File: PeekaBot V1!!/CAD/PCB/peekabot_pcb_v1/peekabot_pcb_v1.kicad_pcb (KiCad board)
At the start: 2 copper layers, 25 parts, among them J1 esp32camright, J2 esp32camleft, J3 USB_B_Micro, J4 Battery Socket, SW1 SW_Push, SW2 SW_Push, U1 IP5306

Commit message: UPDATED PCB-MARK-1!!!
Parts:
- added REF**: M2, MountingHole:MountingHole_2.2mm_M2, F.Cu at (128.5, 56.0)
- added REF**: M2, MountingHole:MountingHole_2.2mm_M2, F.Cu at (156.5, 56.0)
- added REF**: M2, MountingHole:MountingHole_2.2mm_M2, F.Cu at (128.5, 99.5)
- added REF**: M2, MountingHole:MountingHole_2.2mm_M2, F.Cu at (156.5, 99.5)
- moved D3 33.0 mm to (150.0, 67.0), turned to 90 degrees
- moved D2 31.0 mm to (144.0, 63.5)
- moved KEY 24.9 mm to (135.4, 98.8)
- moved J4 23.9 mm to (134.8, 61.0)
- moved R5 23.4 mm to (135.9, 79.5), turned to 180 degrees
- moved J3 22.3 mm to (149.0, 56.7), turned to 180 degrees
- moved C7 18.8 mm to (136.0, 77.0)
- moved J1 18.8 mm to (153.0, 67.0)
- moved J2 17.8 mm to (131.5, 84.5), turned to 180 degrees
- moved U1 17.1 mm to (142.7, 68.1), turned to 180 degrees
- moved IO0 16.6 mm to (150.6, 99.2)
- moved R2 16.2 mm to (145.0, 72.5)
- moved R3 13.7 mm to (140.0, 85.0), turned to 180 degrees
- moved C6 12.0 mm to (135.9, 74.5), turned to 180 degrees
- moved C4 11.9 mm to (136.0, 66.5)
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- renumbered SW1 to IO0, SW2 to KEY
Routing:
- net GND: track 0.00 -> 99.4 mm, vias 0 -> 1
- net BAT: track 0.00 -> 46.8 mm, vias 0 -> 5
- net (no net): track 0.00 -> 44.9 mm, vias 0 -> 7
- net io0: track 0.00 -> 33.7 mm
- net 5V: track 0.00 -> 29.4 mm, vias 0 -> 2
- net Net-(U1-KEY): track 0.00 -> 22.2 mm
- net Net-(R4-Pad2): track 0.00 -> 20.2 mm
- net Net-(J3-VBUS): track 0.00 -> 19.8 mm
- net Net-(U1-SW): track 0.00 -> 12.9 mm, vias 0 -> 2
- net Net-(C5-Pad1): track 0.00 -> 12.6 mm
- net Net-(D3-A): track 0.00 -> 7.99 mm, vias 0 -> 2
- net VCC: track 0.00 -> 7.08 mm
- net Net-(D2-A): track 0.00 -> 6.49 mm
- net Net-(C7-Pad1): track 0.00 -> 2.54 mm
- net Net-(D1-A): track 0.00 -> 2.18 mm
- added copper zone on F.Cu, net GND
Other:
- board outline added: 34.5 x 49.5 mm

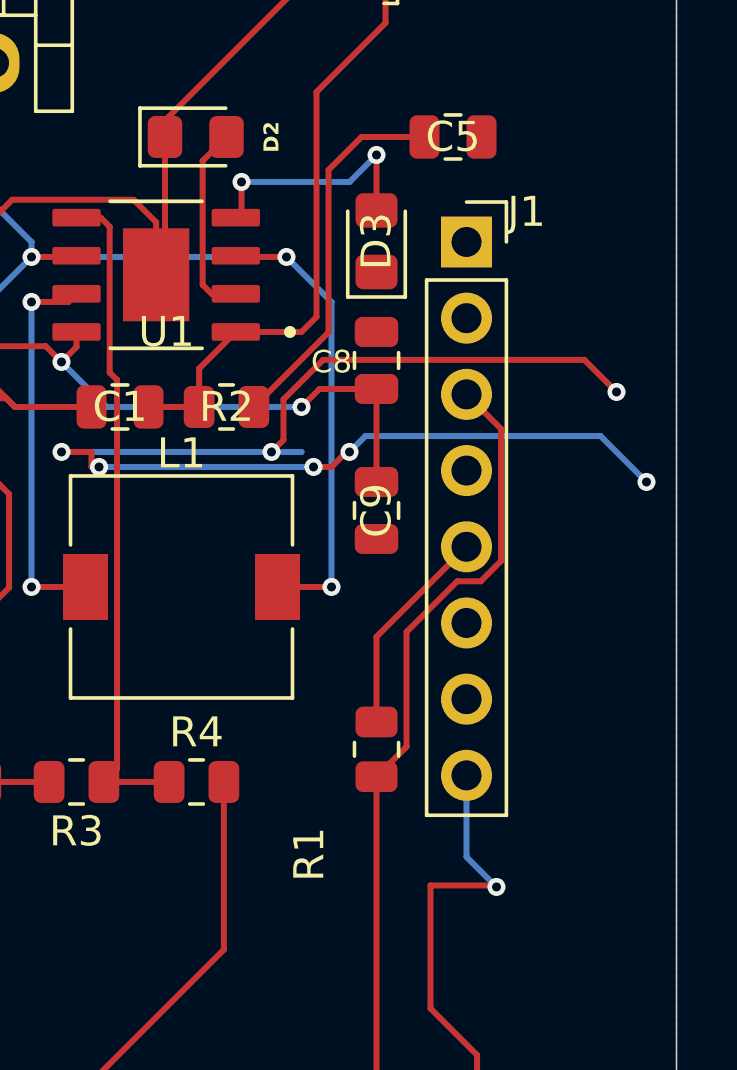
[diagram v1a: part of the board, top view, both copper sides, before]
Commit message: PCB AND 3D DESIGN WORK
started 3d printable enclosure design for the project and corrected a majour spacing error in the PCB
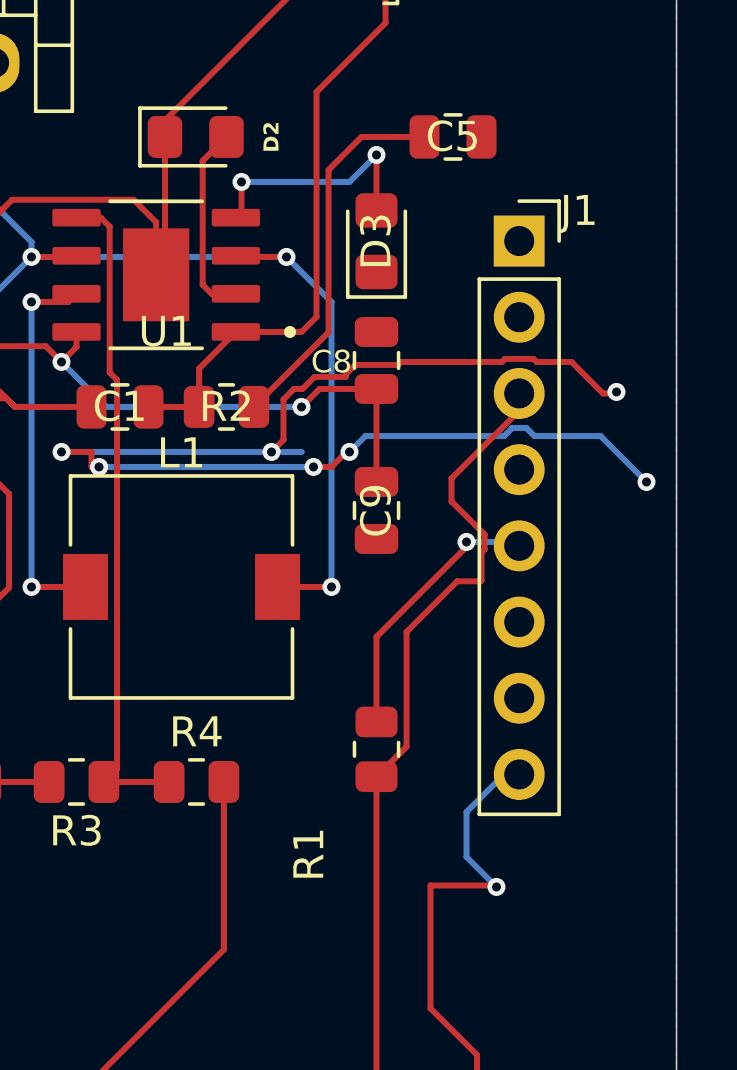
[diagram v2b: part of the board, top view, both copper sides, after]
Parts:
- moved J1 1.76 mm to (154.8, 67.0)
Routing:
- net VCC: track 7.08 -> 9.05 mm, vias 0 -> 1
- net GND: track 99.4 -> 100.5 mm
- net io0: track 33.7 -> 34.4 mm
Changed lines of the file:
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@@
 			(drillshape 0)
 			(scaleselection 1)
-			(outputdirectory "")
+			(outputdirectory "./")
 		)
 	)
@@
 	(footprint "Connector_PinSocket_2.54mm:PinSocket_1x08_P2.54mm_Vertical"
 		(layer "F.Cu")
-		(at 153 67)
+		(at 154.757 66.969534)
 		(descr "Through hole straight socket strip, 1x08, 2.54mm pitch, single row (from Kicad 4.0.7), script generated")
 		(tags "Through hole socket strip THT 1x08 2.54mm single row")
@@
 	)
 	(segment
+		(start 149.28984 71.099)
+		(end 148.974 71.41484)
+		(width 0.2)
+		(layer "F.Cu")
+		(net 0)
+	)
+	(segment
 		(start 148.5 74.5)
 		(end 149 74)
@@
 	)
 	(segment
-		(start 158 72)
-		(end 156.929 70.929)
+		(start 150.80916 71)
+		(end 150.71016 71.099)
 		(width 0.2)
 		(layer "F.Cu")
@@
 	)
 	(segment
-		(start 146.899 72.251057)
-		(end 146.899 73.601)
+		(start 155.23376 70.898534)
+		(end 154.28024 70.898534)
+		(width 0.2)
+		(layer "F.Cu")
+		(net 0)
+	)
+	(segment
+		(start 147.5339 71.899)
+		(end 147.251057 71.899)
 		(width 0.2)
 		(layer "F.Cu")
@@
 	)
 	(segment
-		(start 156.929 70.929)
-		(end 148.221057 70.929)
+		(start 148.974 71.41484)
+		(end 148.974 71.499)
+		(width 0.2)
+		(layer "F.Cu")
+		(net 0)
+	)
+	(segment
+		(start 147.251057 71.899)
+		(end 146.899 72.251057)
+		(width 0.2)
+		(layer "F.Cu")
+		(net 0)
+	)
+	(segment
+		(start 155.335226 71)
+		(end 155.23376 70.898534)
+		(width 0.2)
+		(layer "F.Cu")
+		(net 0)
+	)
+	(segment
+		(start 157.950466 72.049534)
+		(end 157.549534 72.049534)
+		(width 0.2)
+		(layer "F.Cu")
+		(net 0)
+	)
+	(segment
+		(start 148.974 71.499)
+		(end 147.9339 71.499)
 		(width 0.2)
 		(layer "F.Cu")
@@
 	)
 	(segment
+		(start 156.5 71)
+		(end 155.335226 71)
+		(width 0.2)
+		(layer "F.Cu")
+		(net 0)
+	)
+	(segment
+		(start 154.178774 71)
+		(end 150.80916 71)
+		(width 0.2)
+		(layer "F.Cu")
+		(net 0)
+	)
+	(segment
+		(start 146.899 72.251057)
+		(end 146.899 73.601)
+		(width 0.2)
+		(layer "F.Cu")
+		(net 0)
+	)
+	(segment
 		(start 147.9 74.5)
 		(end 148.5 74.5)
@@
 	)
 	(segment
+		(start 157.549534 72.049534)
+		(end 156.5 71)
+		(width 0.2)
+		(layer "F.Cu")
+		(net 0)
+	)
+	(segment
 		(start 140.5 74)
 		(end 139.5 74)
@@
 	)
 	(segment
+		(start 158 72)
+		(end 157.950466 72.049534)
+		(width 0.2)
+		(layer "F.Cu")
+		(net 0)
+	)
+	(segment
+		(start 147.9339 71.499)
+		(end 147.5339 71.899)
+		(width 0.2)
+		(layer "F.Cu")
+		(net 0)
+	)
+	(segment
 		(start 140.5 74.5)
 		(end 140.95 74.5)
@@
 	)
 	(segment
-		(start 148.221057 70.929)
-		(end 146.899 72.251057)
+		(start 154.28024 70.898534)
+		(end 154.178774 71)
+		(width 0.2)
+		(layer "F.Cu")
+		(net 0)
+	)
+	(segment
+		(start 150.71016 71.099)
+		(end 149.28984 71.099)
 		(width 0.2)
 		(layer "F.Cu")
@@
 	)
 	(segment
-		(start 149.631 73.469)
-		(end 157.469 73.469)
+		(start 154.51824 73.200534)
+		(end 154.99576 73.200534)
 		(width 0.2)
 		(layer "B.Cu")
@@
 	)
 	(segment
+		(start 139.5 74)
+		(end 147.5 74)
+		(width 0.2)
+		(layer "B.Cu")
+		(net 0)
+	)
+	(segment
 		(start 149.1 74)
 		(end 149.631 73.469)
@@
 	)
 	(segment
-		(start 139.5 74)
-		(end 147.5 74)
+		(start 149.631 73.469)
+		(end 154.249774 73.469)
 		(width 0.2)
 		(layer "B.Cu")
@@
 	)
 	(segment
+		(start 155.264226 73.469)
+		(end 157.469 73.469)
+		(width 0.2)
+		(layer "B.Cu")
+		(net 0)
+	)
+	(segment
+		(start 154.99576 73.200534)
+		(end 155.264226 73.469)
+		(width 0.2)
+		(layer "B.Cu")
+		(net 0)
+	)
+	(segment
 		(start 147.5 74)
 		(end 146.5 74)
@@
 	)
 	(segment
+		(start 154.249774 73.469)
+		(end 154.51824 73.200534)
+		(width 0.2)
+		(layer "B.Cu")
+		(net 0)
+	)
+	(segment
 		(start 148 62)
 		(end 148 69.5)
@@
 	)
 	(segment
-		(start 154 88.5)
+		(start 153 86)
 		(end 153 87.5)
 		(width 0.2)
@@
 	)
 	(segment
+		(start 154.250466 84.749534)
+		(end 153 86)
+		(width 0.2)
+		(layer "B.Cu")
+		(net 2)
+	)
+	(segment
 		(start 153 87.5)
-		(end 153 84.78)
+		(end 154 88.5)
+		(width 0.2)
+		(layer "B.Cu")
+		(net 2)
+	)
+	(segment
+		(start 154.757 84.749534)
+		(end 154.250466 84.749534)
 		(width 0.2)
 		(layer "B.Cu")
@@
 	)
 	(segment
+		(start 153 77.16)
+		(end 153 77)
+		(width 0.2)
+		(layer "F.Cu")
+		(net 11)
+	)
+	(segment
 		(start 150 83)
 		(end 150 80.16)
@@
 		(net 11)
 	)
+	(via
+		(at 153 77)
+		(size 0.6)
+		(drill 0.3)
+		(layers "F.Cu" "B.Cu")
+		(net 11)
+	)
+	(segment
+		(start 153 77)
+		(end 154.627466 77)
+		(width 0.2)
+		(layer "B.Cu")
+		(net 11)
+	)
+	(segment
+		(start 154.627466 77)
+		(end 154.757 77.129534)
+		(width 0.2)
+		(layer "B.Cu")
+		(net 11)
+	)
+	(segment
+		(start 150 96.9)
+		(end 148.5 98.4)
+		(width 0.2)
+		(layer "F.Cu")
+		(net 12)
+	)
+	(segment
+		(start 153.5 78.28776)
+		(end 153.47676 78.311)
+		(width 0.2)
+		(layer "F.Cu")
+		(net 12)
+	)
+	(segment
+		(start 153.601 77.248943)
+		(end 153.5 77.349943)
+		(width 0.2)
+		(layer "F.Cu")
+		(net 12)
+	)
+	(segment
+		(start 150 84.825)
+		(end 150 96.9)
+		(width 0.2)
+		(layer "F.Cu")
+		(net 12)
+	)
+	(segment
+		(start 153.601 76.751057)
+		(end 153.601 77.248943)
+		(width 0.2)
+		(layer "F.Cu")
+		(net 12)
+	)
+	(segment
+		(start 152.5 75.650057)
+		(end 153.601 76.751057)
+		(width 0.2)
+		(layer "F.Cu")
+		(net 12)
+	)
 	(segment
 		(start 151.001 83.824)
@@
 	)
 	(segment
-		(start 150 96.9)
-		(end 148.5 98.4)
+		(start 154.757 72.049534)
+		(end 154.757 72.625)
 		(width 0.2)
 		(layer "F.Cu")
@@
 	)
 	(segment
-		(start 150 84.825)
-		(end 150 96.9)
+		(start 153.5 77.349943)
+		(end 153.5 78.28776)
 		(width 0.2)
 		(layer "F.Cu")
@@
 	)
 	(segment
-		(start 153 72.08)
-		(end 154.151 73.231)
+		(start 152.5 74.882)
+		(end 152.5 75.650057)
 		(width 0.2)
 		(layer "F.Cu")
@@
 	)
 	(segment
-		(start 154.151 73.231)
-		(end 154.151 77.63676)
-		(width 0.2)
-		(layer "F.Cu")
-		(net 12)
-	)
-	(segment
-		(start 154.151 77.63676)
-		(end 153.47676 78.311)
+		(start 154.757 72.625)
+		(end 152.5 74.882)
 		(width 0.2)
 		(layer "F.Cu")

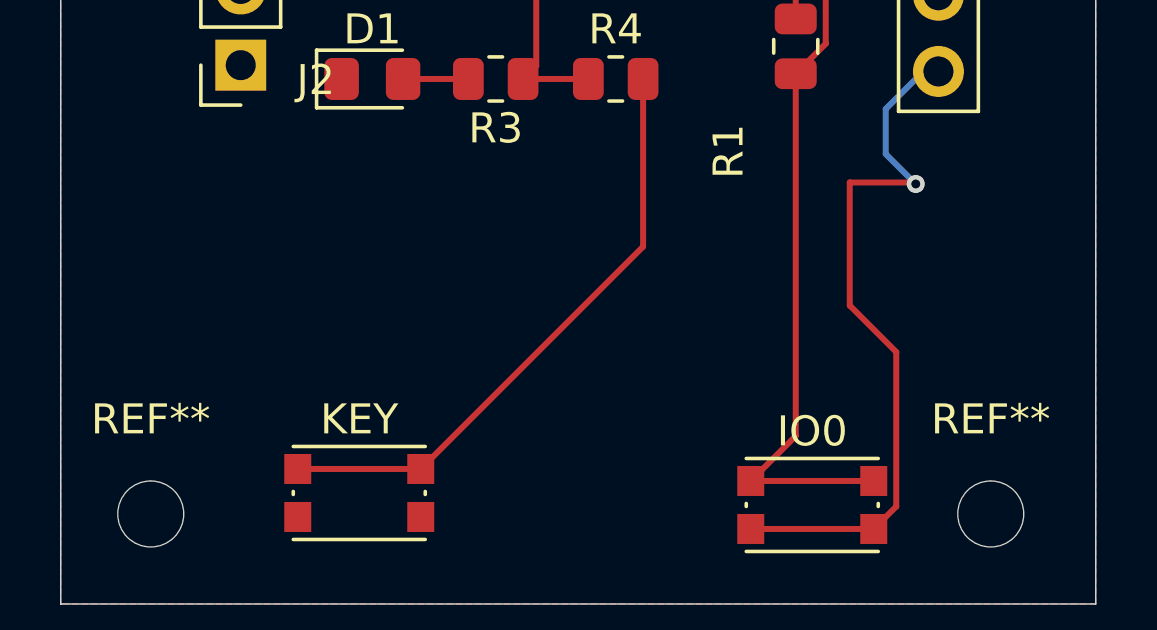
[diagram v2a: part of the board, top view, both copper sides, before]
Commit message: Upodated code,3d desig,pcb
improved the code
improved and iterated the 3d design
rendered all the 3d parts
added name and hack club logo in the pcb
organized all the file
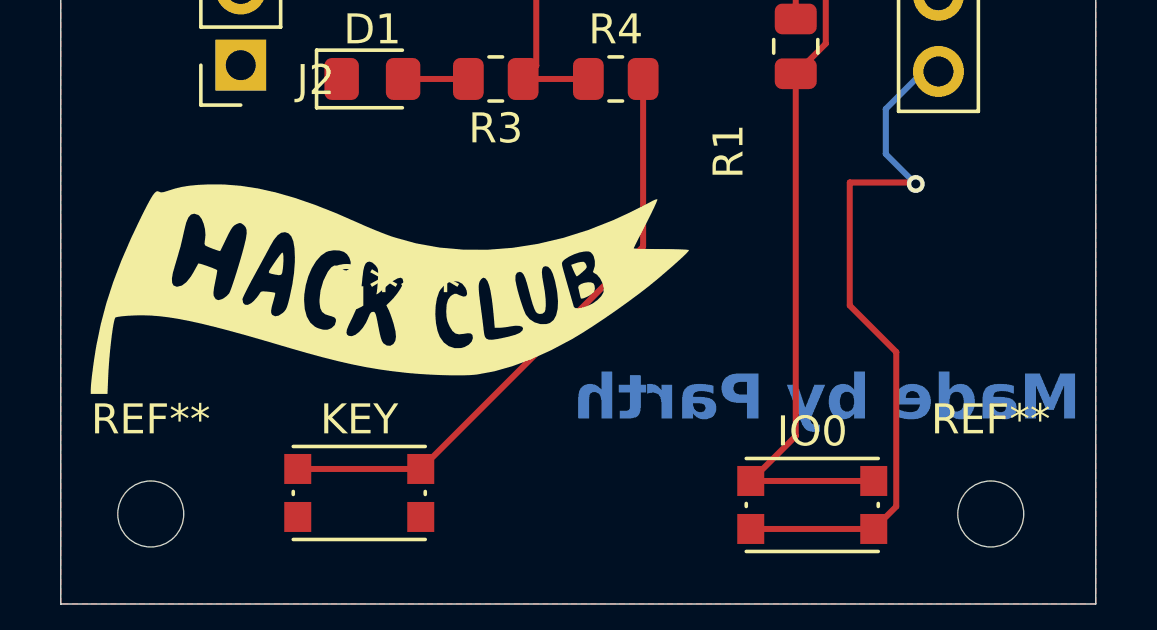
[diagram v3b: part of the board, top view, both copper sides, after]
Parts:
- added G***: LOGO, hackclublogo:hackclublogo, F.Cu at (136.5, 92.0)
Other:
- board text added: "Made by Parth"
